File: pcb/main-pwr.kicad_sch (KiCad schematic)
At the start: 6 parts, among them U2 ADP5054

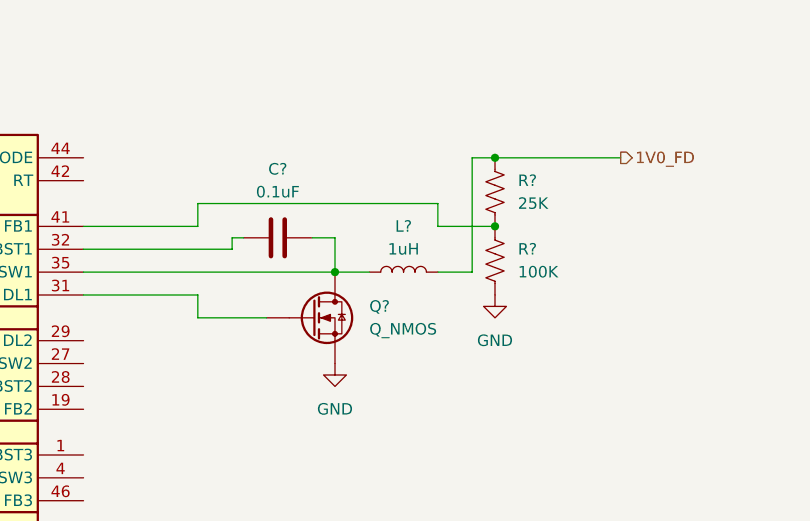
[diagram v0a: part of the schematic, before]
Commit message: updated power hierarchy and sims
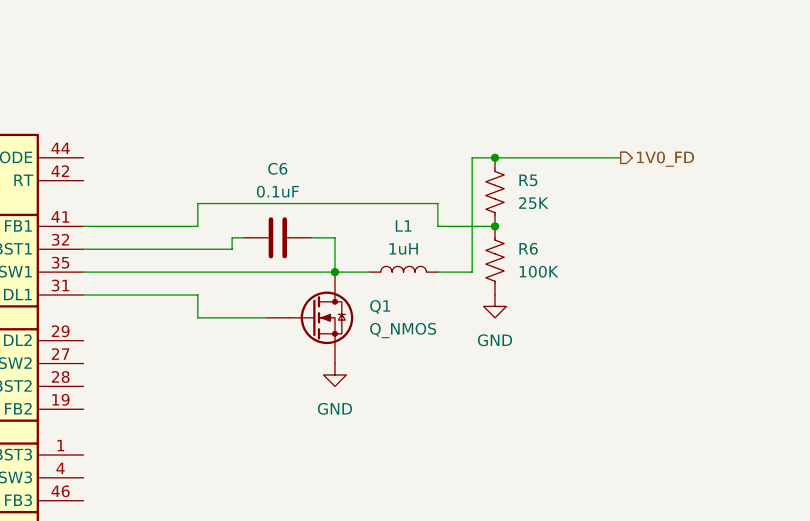
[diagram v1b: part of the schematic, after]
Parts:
- gave numbers to parts that had none: 5
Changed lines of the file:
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@@
 		(dnp no)
 		(fields_autoplaced yes)
-		(property "Reference" "C?"
+		(property "Reference" "C6"
 			(at 161.29 50.8 90)
 			(effects
@@
 			(project ""
 				(path "/e63e39d7-6ac0-4ffd-8aa3-1841a4541b55/f9ebb56c-78c7-42ac-bc19-ccbf788f5318"
-					(reference "C?")
+					(reference "C6")
 					(unit 1)
 				)
@@
 		(dnp no)
 		(fields_autoplaced yes)
-		(property "Reference" "Q?"
+		(property "Reference" "Q1"
 			(at 171.45 66.0399 0)
 			(effects
@@
 			(project ""
 				(path "/e63e39d7-6ac0-4ffd-8aa3-1841a4541b55/f9ebb56c-78c7-42ac-bc19-ccbf788f5318"
-					(reference "Q?")
+					(reference "Q1")
 					(unit 1)
 				)
@@
 		(dnp no)
 		(fields_autoplaced yes)
-		(property "Reference" "R?"
+		(property "Reference" "R5"
 			(at 187.96 52.0699 0)
 			(effects
@@
 			(project "RPi-HwAB-1"
 				(path "/e63e39d7-6ac0-4ffd-8aa3-1841a4541b55/f9ebb56c-78c7-42ac-bc19-ccbf788f5318"
-					(reference "R?")
+					(reference "R5")
 					(unit 1)
 				)
@@
 		(dnp no)
 		(fields_autoplaced yes)
-		(property "Reference" "R?"
+		(property "Reference" "R6"
 			(at 187.96 59.6899 0)
 			(effects
@@
 			(project ""
 				(path "/e63e39d7-6ac0-4ffd-8aa3-1841a4541b55/f9ebb56c-78c7-42ac-bc19-ccbf788f5318"
-					(reference "R?")
+					(reference "R6")
 					(unit 1)
 				)
@@
 		(dnp no)
 		(fields_autoplaced yes)
-		(property "Reference" "L?"
+		(property "Reference" "L1"
 			(at 175.26 57.15 90)
 			(effects
@@
 			(project ""
 				(path "/e63e39d7-6ac0-4ffd-8aa3-1841a4541b55/f9ebb56c-78c7-42ac-bc19-ccbf788f5318"
-					(reference "L?")
-					(unit 1)
-				)
+					(reference "L1")
+					(unit 1)
+				)

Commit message: edits to simulations
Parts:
- removed C6: 0.1uF, Capacitor_SMD:C_0402_1005Metric, symbol Device:C
- removed L1: 1uH, Inductor_SMD:L_0402_1005Metric, symbol Device:L
- removed Q1: Q_NMOS, symbol Device:Q_NMOS
- removed R5: 25K, Resistor_SMD:R_0402_1005Metric, symbol Device:R_US
- removed R6: 100K, Resistor_SMD:R_0402_1005Metric, symbol Device:R_US
- added C? (x4): 10uF, symbol Device:C
- added C? (x4): 2.2nF, symbol Device:C
- added C? (x2): 0.1uF, symbol Device:C
- added L? (x2): 1uF, symbol Device:L
- added R?: 120K, symbol Device:R_US
- added R? (x4): 10K, symbol Device:R_US
- added R?: 15K, symbol Device:R_US
- added R?: 31.6K, symbol Device:R_US
- added R? (x2): 30K, symbol Device:R_US
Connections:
- net 1V0_FD: now also L?.2, R?.1
- net 1V2_MGT: now also L?.2, R?.1
- net 5V0: now also C?.1, C?.1, C?.1, C?.1
- net GND: now also U2.10 (PGND4), U2.11 (PGND4), U2.18 (CFG12), U2.2 (PGND3), U2.3 (PGND3), U2.30 (PGND), U2.44 (SYNC/MODE), U2.49 (EPAD), C?.2, C?.2, C?.2, C?.2, C?.2, C?.2, C?.2, C?.2, R?.1, R?.2, R?.2
- net at U2.15 (COMP4): now also R?.2
- net at U2.19 (FB2): now also R?.1, R?.2
- net at U2.20 (COMP2): now also R?.2
- net at U2.25 (SW2), U2.26 (SW2), U2.27 (SW2): now also C?.2, L?.1
- net at U2.28 (BST2): now also C?.1
- net at U2.32 (BST1): now also C?.1
- net at U2.33 (SW1), U2.34 (SW1): now also U2.41 (FB1), R?.1, R?.2; no longer U2.35 (SW1)
- net at U2.40 (COMP1): now also R?.2
- net at U2.42 (RT): now also R?.2
- net at U2.47 (COMP3): now also R?.2
- new net: C?.2, L?.1, U2.35 (SW1)
- new net: C?.1, R?.1 (x4)
- no-connect marks 0 -> 2
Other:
- moved on the sheet: U2

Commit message: power supply template~?
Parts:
- added C? (x2): 0.1uF, symbol Device:C
- added L? (x2): 1uF, symbol Device:L
- added R?: 120K, symbol Device:R_US
- added R? (x2): 30K, symbol Device:R_US
- added R?: 15K, symbol Device:R_US
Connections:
- net GND: now also R?.2, R?.2
- net at U2.1 (BST3): now also C?.1
- net at U2.12 (BST4): now also C?.1
- net at U2.16 (FB4): now also R?.1, R?.2
- net at U2.4 (SW3), U2.5 (SW3): now also C?.2, L?.1
- net at U2.46 (FB3): now also R?.1, R?.2
- net at U2.8 (SW4), U2.9 (SW4): now also C?.2, L?.1
- new net: L?.2, R?.1 (x2)

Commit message: decoupling
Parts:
- L? (x4): value 1uF -> 1uH
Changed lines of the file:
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@@
 			)
 		)
-		(property "Value" "1uF"
+		(property "Value" "1uH"
 			(at 199.39 110.49 90)
 			(effects
@@
 			)
 		)
-		(property "Value" "1uF"
+		(property "Value" "1uH"
 			(at 227.33 86.36 90)
 			(effects
@@
 			)
 		)
-		(property "Value" "1uF"
+		(property "Value" "1uH"
 			(at 220.98 36.83 90)
 			(effects
@@
 			)
 		)
-		(property "Value" "1uF"
+		(property "Value" "1uH"
 			(at 199.39 54.61 90)
 			(effects
@@
 		(on_board yes)
 		(dnp no)
-		(fields_autoplaced yes)
 		(property "Reference" "C?"
 			(at 210.82 31.75 90)

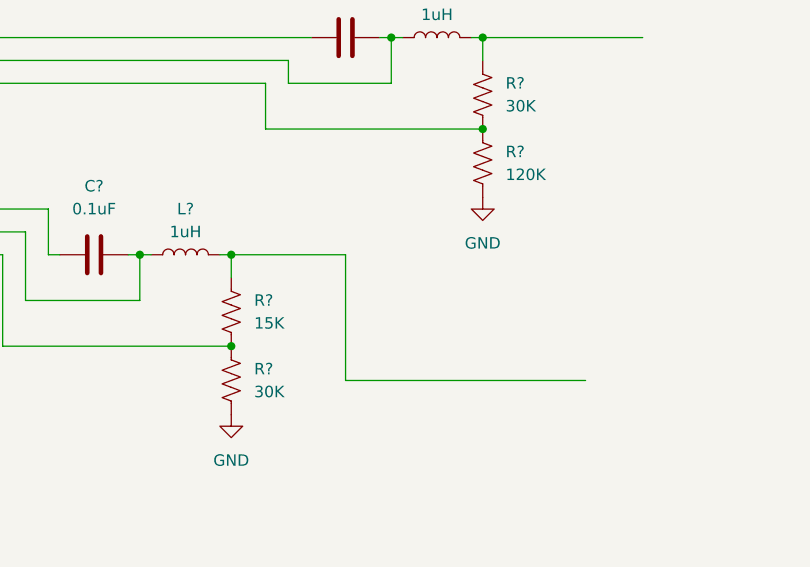
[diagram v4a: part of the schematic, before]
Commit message: buck outputs
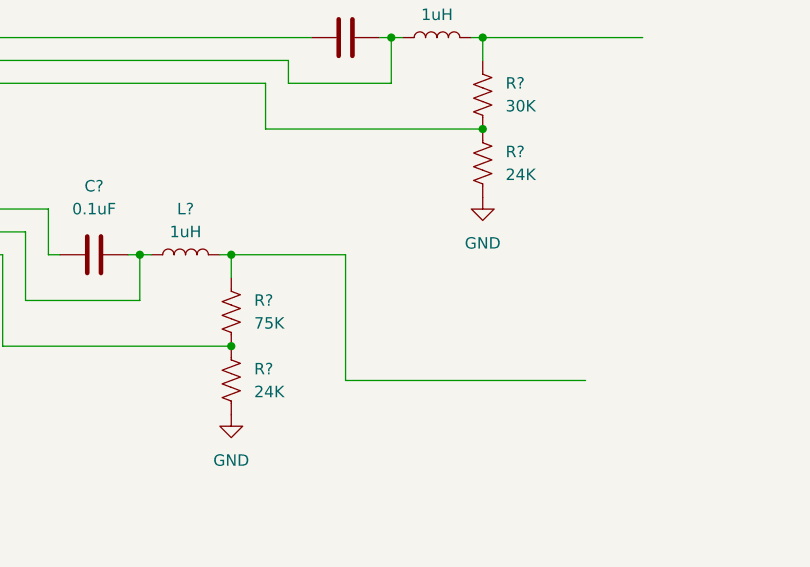
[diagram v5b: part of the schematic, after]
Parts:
- R?: value 120K -> 24K
- R?: value 30K -> 24K
- R?: value 15K -> 75K
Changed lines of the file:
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@@
 			)
 		)
-		(property "Value" "120K"
+		(property "Value" "24K"
 			(at 234.95 104.1399 0)
 			(effects
@@
 			)
 		)
-		(property "Value" "30K"
+		(property "Value" "24K"
 			(at 207.01 128.2699 0)
 			(effects
@@
 			)
 		)
-		(property "Value" "15K"
+		(property "Value" "75K"
 			(at 207.01 120.6499 0)
 			(effects

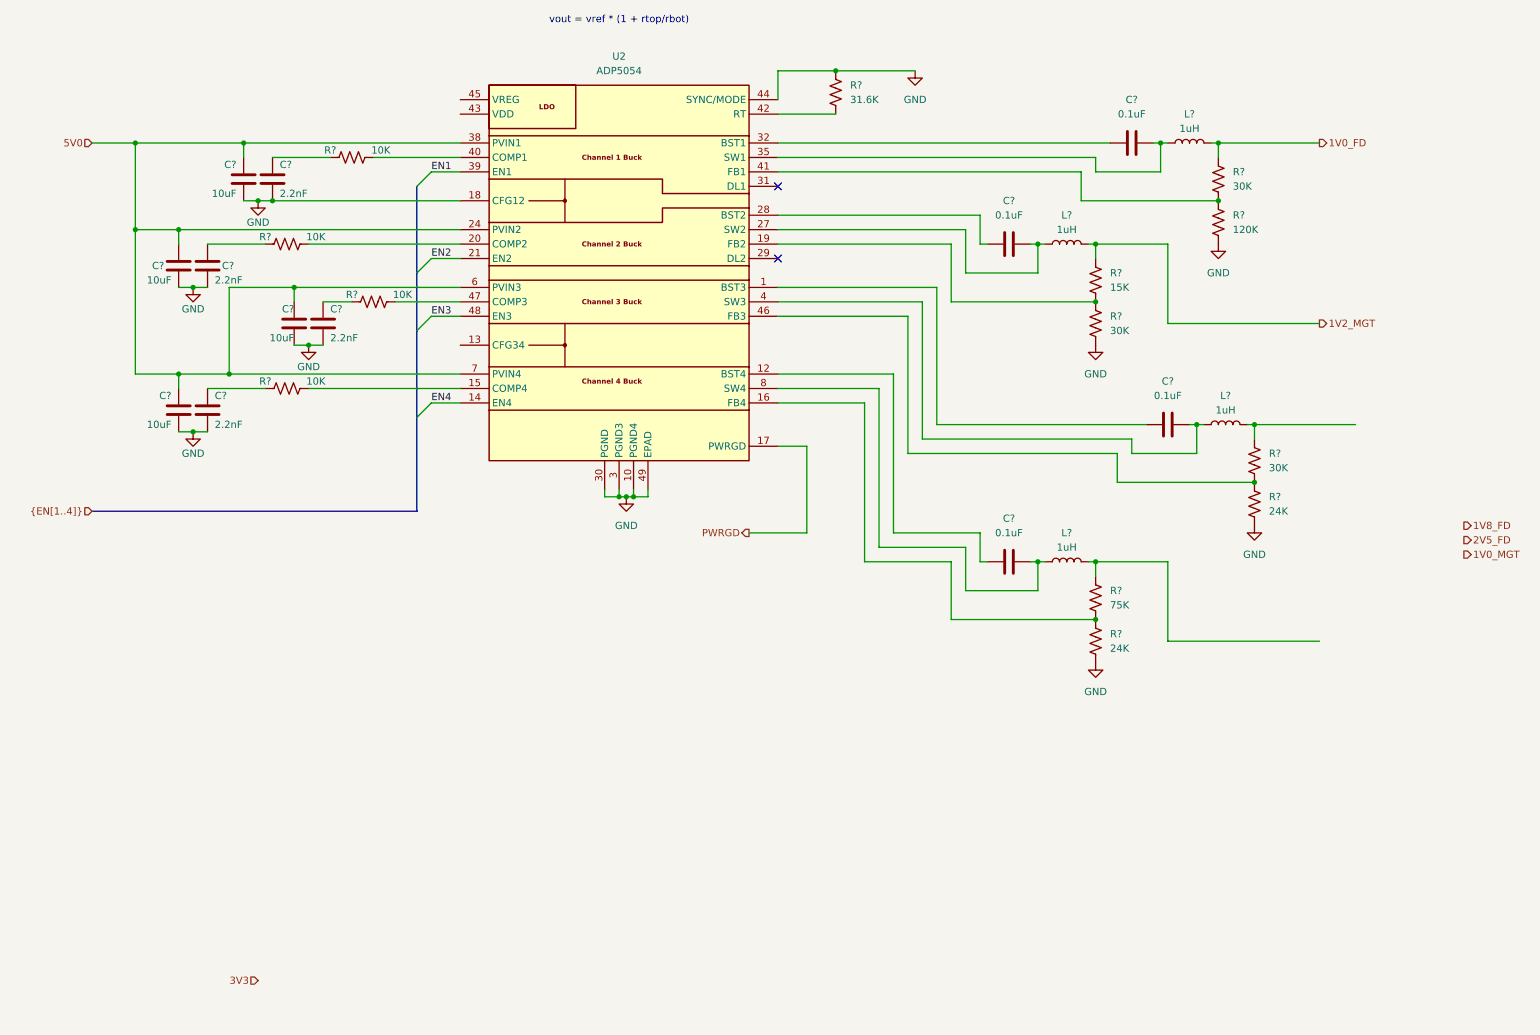
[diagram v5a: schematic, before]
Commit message: restructured power hierarchy
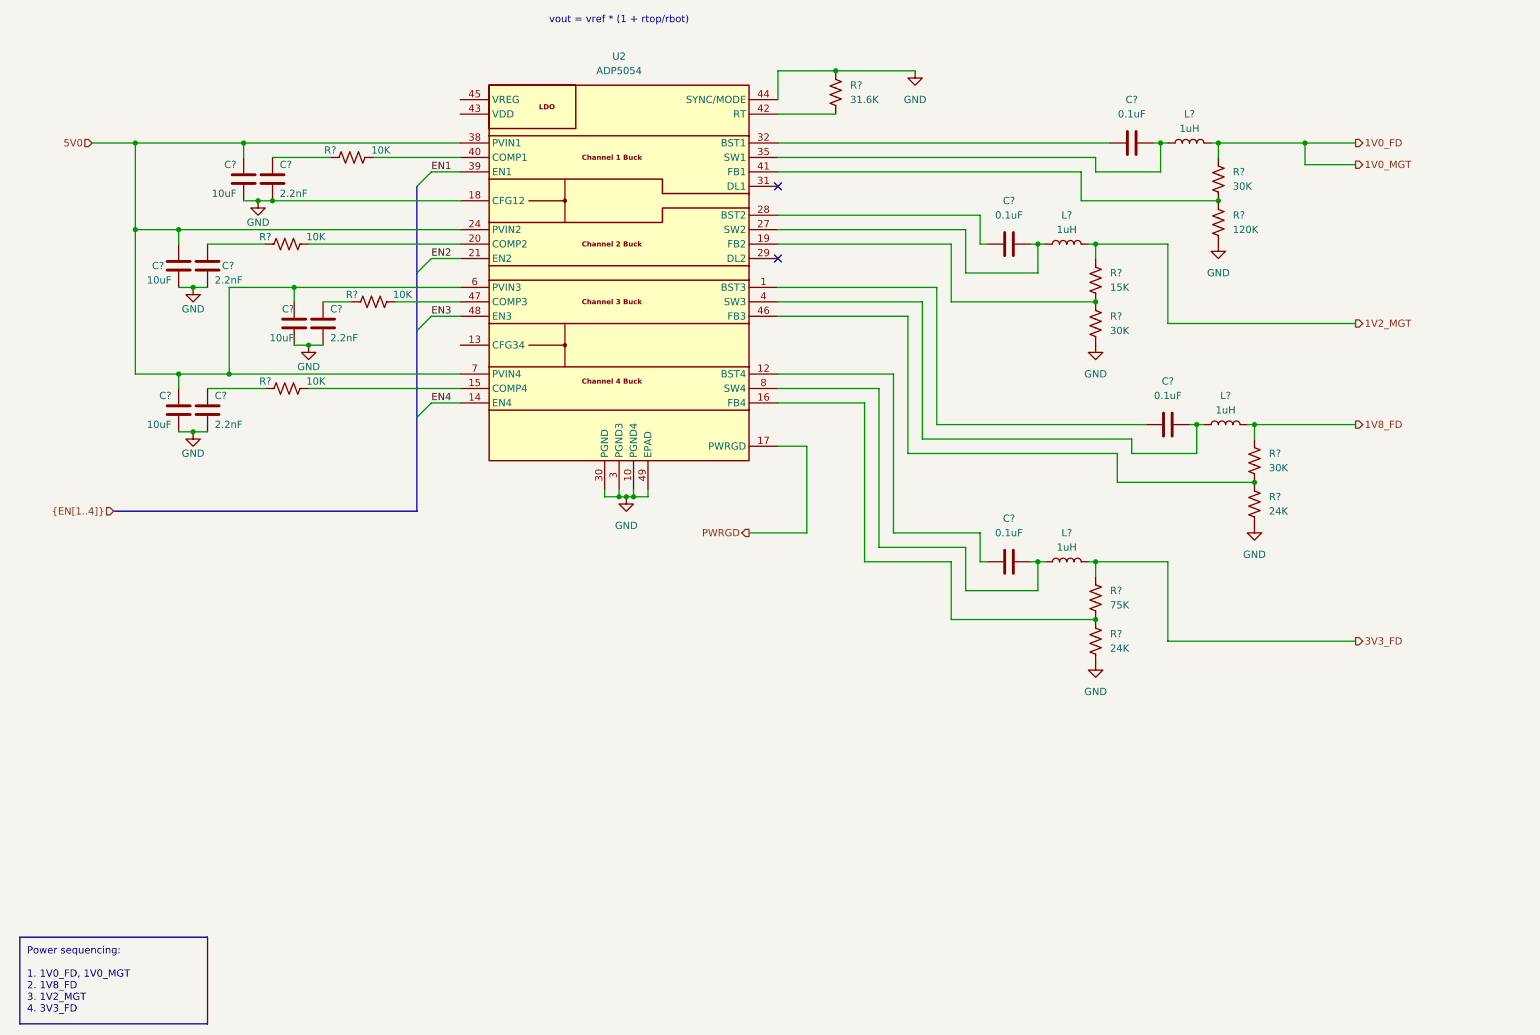
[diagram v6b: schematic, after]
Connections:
- net 1V8_FD: now also L?.2, R?.1
- net 3V3_FD: now reaches L?.2, R?.1
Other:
- note added: "Power sequencing: 1. 1V0_FD, 1V0_MGT 2. 1V8_FD 3. 1V2_MGT 4. 3V3_FD"
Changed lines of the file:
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@@
 		(company "Andre S Winkel")
+	)
+	(rectangle
+		(start 15.24 179.07)
+		(end 48.26 194.31)
+		(stroke
+			(width 0)
+			(type default)
+		)
+		(fill
+			(type none)
+		)
 	)
 	(text "vout = vref * (1 + rtop/rbot)"
@@
 		)
 	)
+	(text "Power sequencing: \n\n1. 1V0_FD, 1V0_MGT\n2. 1V8_FD\n3. 1V2_MGT\n4. 3V3_FD"
+		(exclude_from_sim no)
+		(at 16.51 186.69 0)
+		(effects
+			(font
+				(size 1.27 1.27)
+			)
+			(justify left)
+		)
+	)
 	(junction
 		(at 52.07 80.01)
@@
 	(junction
 		(at 66.04 74.93)
+		(diameter 0)
+		(color 0 0 0 0)
+	)
+	(junction
+		(at 241.3 39.37)
 		(diameter 0)
 		(color 0 0 0 0)
@@
 	(wire
 		(pts
+			(xy 250.19 43.18) (xy 241.3 43.18)
+		)
+		(stroke
+			(width 0)
+			(type default)
+		)
+	)
+	(wire
+		(pts
 			(xy 203.2 57.15) (xy 204.47 57.15)
 		)
@@
 	(wire
 		(pts
-			(xy 217.17 71.12) (xy 243.84 71.12)
+			(xy 217.17 71.12) (xy 250.19 71.12)
 		)
 		(stroke
@@
 	(bus
 		(pts
-			(xy 27.94 104.14) (xy 85.09 104.14)
+			(xy 31.75 104.14) (xy 85.09 104.14)
 		)
 		(stroke
@@
 	(wire
 		(pts
+			(xy 241.3 39.37) (xy 250.19 39.37)
+		)
+		(stroke
+			(width 0)
+			(type default)
+		)
+	)
+	(wire
+		(pts
 			(xy 48.26 82.55) (xy 58.42 82.55)
 		)
@@
 	(wire
 		(pts
+			(xy 241.3 43.18) (xy 241.3 39.37)
+		)
+		(stroke
+			(width 0)
+			(type default)
+		)
+	)
+	(wire
+		(pts
 			(xy 208.28 99.06) (xy 232.41 99.06)
 		)
@@
 	(wire
 		(pts
-			(xy 226.06 39.37) (xy 243.84 39.37)
+			(xy 226.06 39.37) (xy 241.3 39.37)
 		)
 		(stroke
@@
 	(wire
 		(pts
-			(xy 217.17 127) (xy 243.84 127)
+			(xy 217.17 127) (xy 250.19 127)
 		)
 		(stroke
@@
 	(hierarchical_label "1V8_FD"
 		(shape output)
-		(at 269.24 106.68 0)
+		(at 250.19 88.9 0)
 		(effects
 			(font
@@
 	(hierarchical_label "1V0_MGT"
 		(shape output)
-		(at 269.24 111.76 0)
+		(at 250.19 43.18 0)
 		(effects
 			(font
@@
 	(hierarchical_label "1V0_FD"
 		(shape output)
-		(at 243.84 39.37 0)
+		(at 250.19 39.37 0)
 		(effects
 			(font
@@
 	(hierarchical_label "1V2_MGT"
 		(shape output)
-		(at 243.84 71.12 0)
+		(at 250.19 71.12 0)
 		(effects
 			(font
@@
 		)
 	)
-	(hierarchical_label "2V5_FD"
+	(hierarchical_label "3V3_FD"
 		(shape output)
-		(at 269.24 109.22 0)
+		(at 250.19 127 0)
 		(effects
 			(font
@@
 		)
 	)
-	(hierarchical_label "3V3"
+	(hierarchical_label "{EN[1..4]}"
 		(shape input)
-		(at 57.15 186.69 180)
+		(at 31.75 104.14 180)
 		(effects
 			(font
-				(size 1.27 1.27)
-			)
-			(justify right)
-		)
-	)
-	(hierarchical_label "{EN[1..4]}"
-		(shape input)
-		(at 27.94 104.14 180)
-		(effects
-			(font

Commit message: power supply comp abstraction
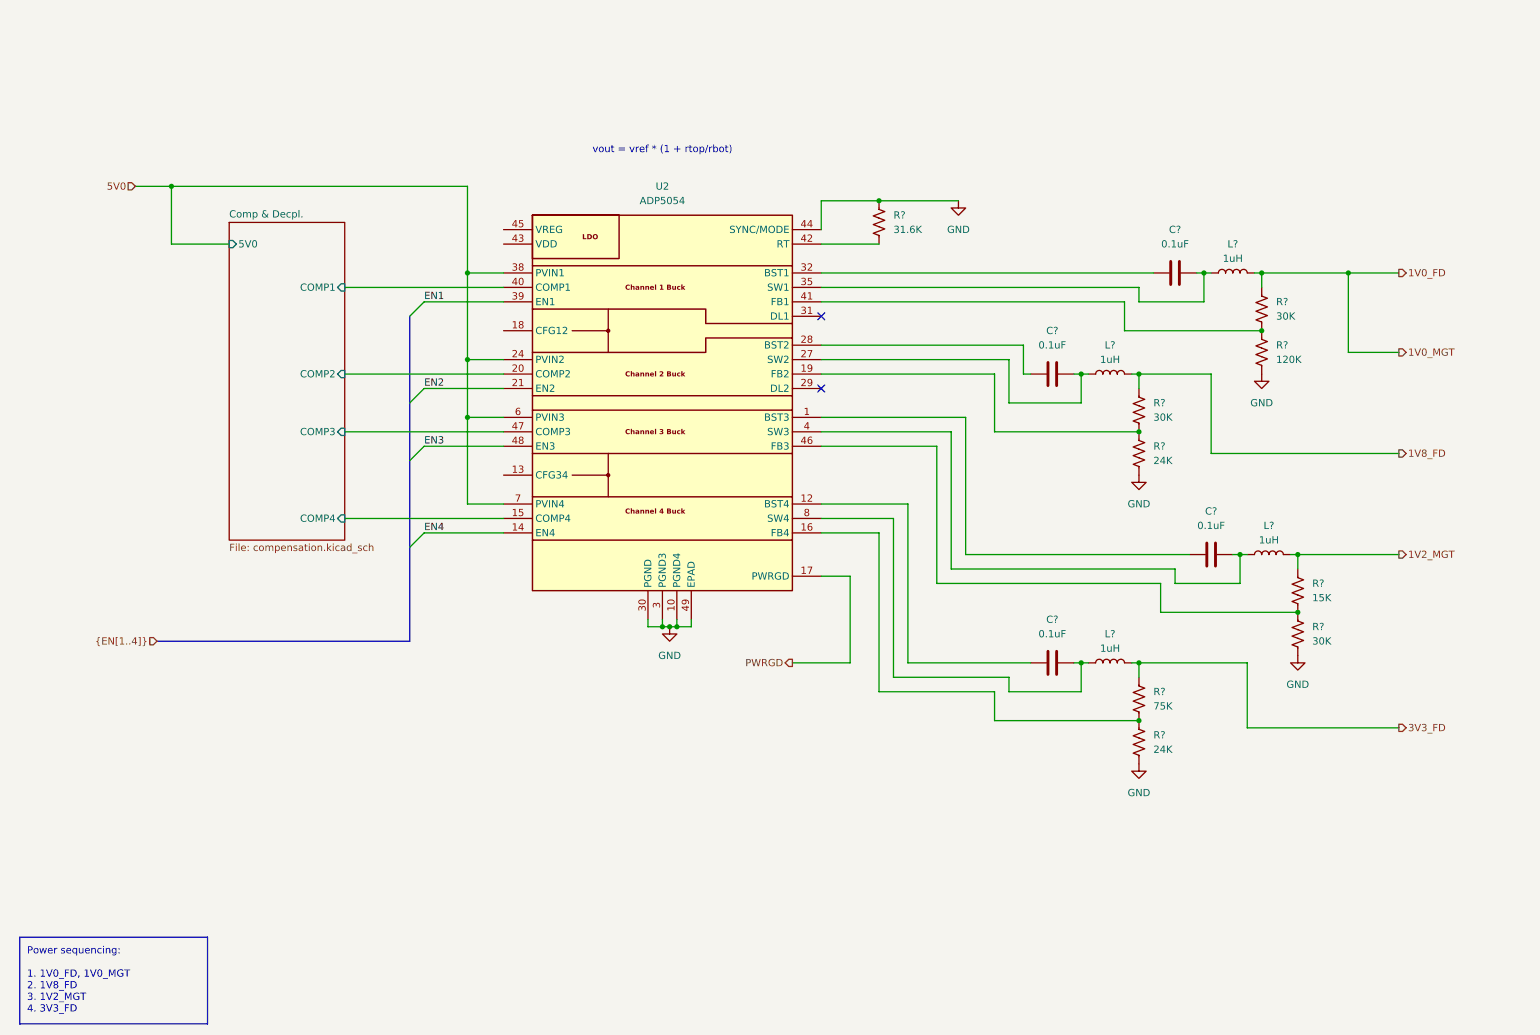
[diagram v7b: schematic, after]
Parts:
- removed C? (x4): 10uF, symbol Device:C
- removed C? (x4): 2.2nF, symbol Device:C
- removed R? (x4): 10K, symbol Device:R_US
- R?: value 24K -> 30K
- R?: value 15K -> 30K
- R?: value 30K -> 15K
- R?: value 30K -> 24K
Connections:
- net 1V2_MGT: now also L?.2, R?.1; no longer L?.2, R?.1
- net 1V8_FD: now also L?.2, R?.1; no longer L?.2, R?.1
- net GND: no longer U2.18 (CFG12)
- net Comp & Decpl./COMP4: now reaches U2.15 (COMP4)
- net Comp & Decpl./COMP2: now reaches U2.20 (COMP2)
- net Comp & Decpl./COMP1: now reaches U2.40 (COMP1)
- net Comp & Decpl./COMP3: now reaches U2.47 (COMP3)
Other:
- added sheet Comp & Decpl. (compensation.kicad_sch)
- moved on the sheet: C?, L?, R?, U2
